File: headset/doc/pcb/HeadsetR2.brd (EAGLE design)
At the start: 85 x 56 mm, 54 parts, among them U1 STM32F405RGT6, U2 MAX17043, U3 MCP73831, U4 MIC5216, U5 MIC5216, U6 MIC5219 3.3V, U7 XBEE, U8 STEVAL-MKI108V2, Y1 8MHz

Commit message: Update headset schematic revision 2 (again), almost ready for route
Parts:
- moved R5 8.91 mm to (81.3, 41.3), turned to 0 degrees
- moved C16 5.99 mm to (75.6, 41.3), turned to 180 degrees
- moved U2 5.68 mm to (72.4, 44.5)
- moved JP3 5.68 mm to (17.8, 43.2), turned to 270 degrees
- moved D1 5.24 mm to (77.5, 44.5), turned to 180 degrees
- moved U3 5.08 mm to (81.9, 45.7)
- moved C21 4.02 mm to (40.6, 52.1)
- moved R6 3.81 mm to (77.5, 47.6), turned to 0 degrees
- moved U5 3.59 mm to (47.6, 50.2), turned to 180 degrees
- moved R1 2.84 mm to (48.3, 40.6), turned to 270 degrees
- moved JP1 2.54 mm to (78.7, 30.5)
- moved C22 2.54 mm to (40.6, 47.0)
- moved C17 2.29 mm to (71.8, 47.6), flipped to the top, turned to 0 degrees
- moved R4 1.27 mm to (71.1, 31.8)
- moved R3 1.27 mm to (71.1, 29.2)
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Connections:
- net !CS!: now also U1.50; no longer U1.33
- net MISO: now also U1.52; no longer U1.35
- net MOSI: now also U1.53; no longer U1.36
- net SCK: now also U1.51; no longer U1.34
- net X_RX: now also U1.16; no longer U1.42
- net X_TX: now also U1.17; no longer U1.43

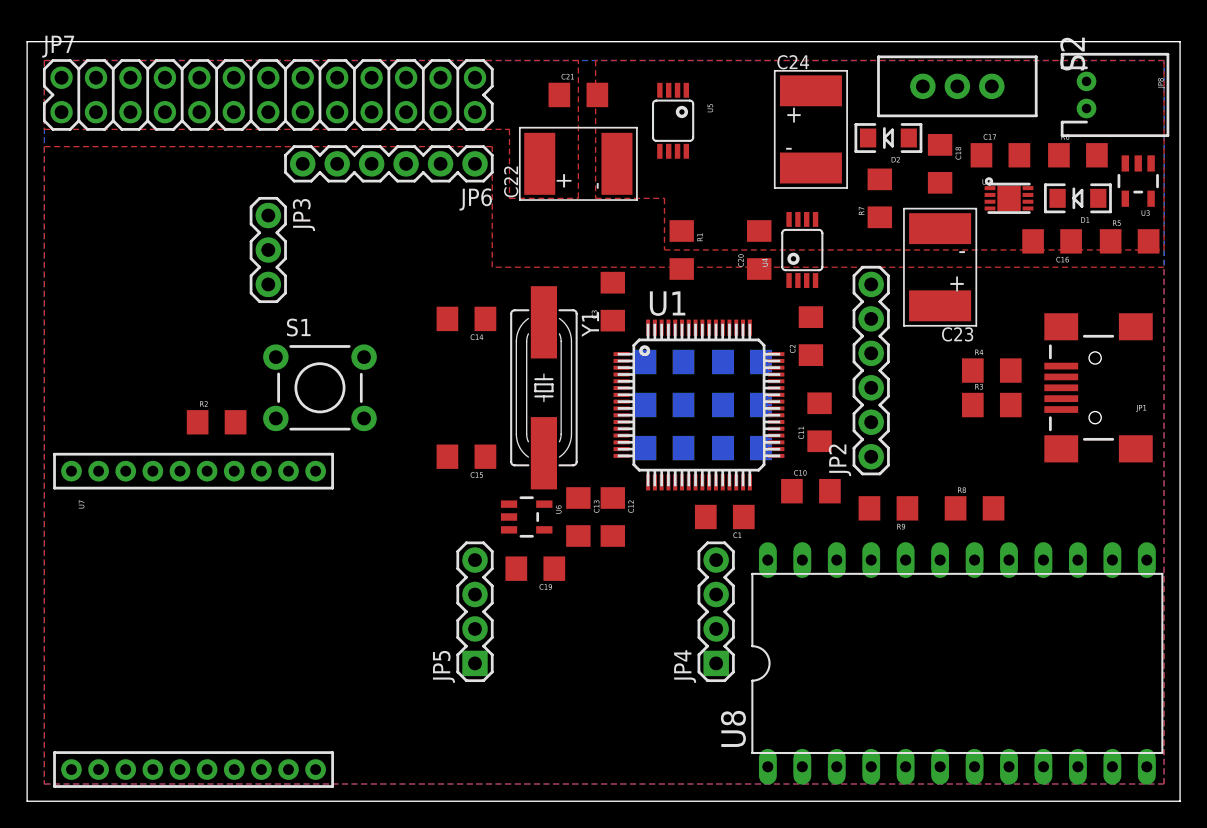
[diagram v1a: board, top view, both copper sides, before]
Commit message: Update schematic revision 2 to fix the issues described in lab notebook
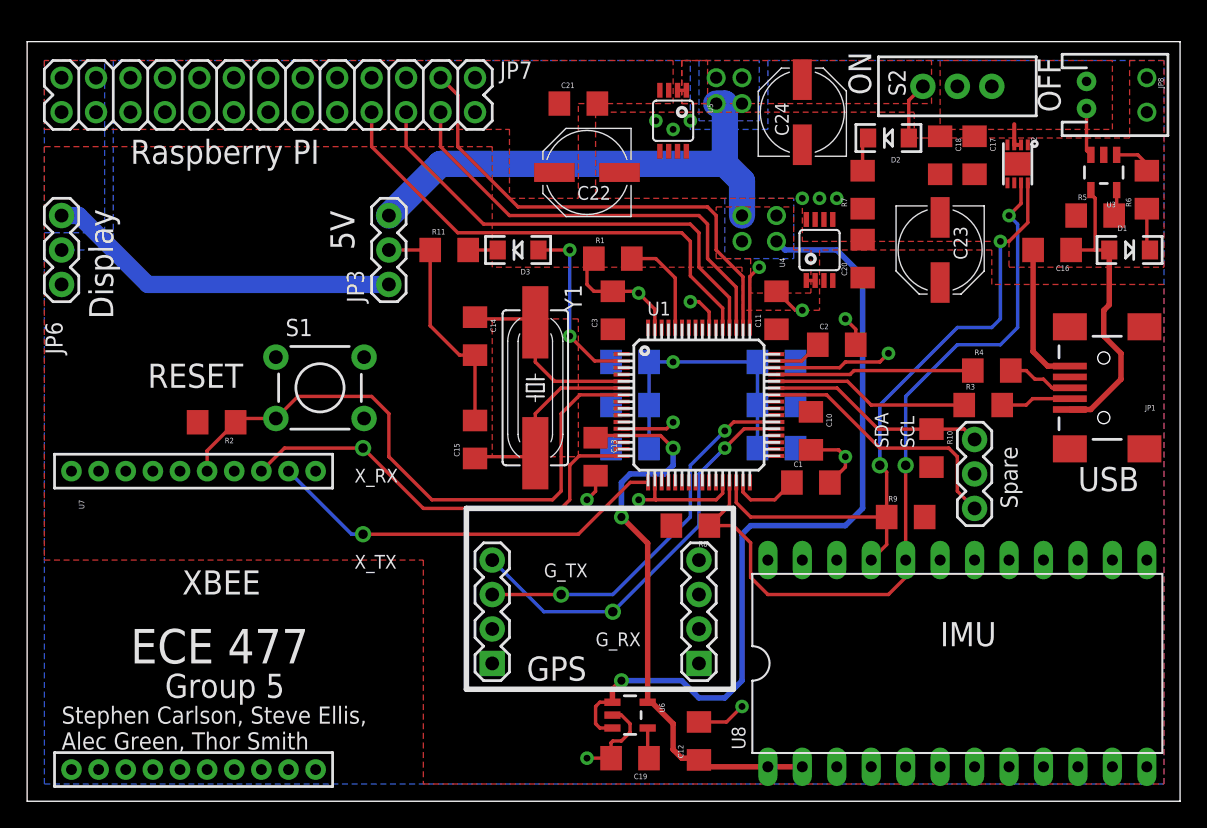
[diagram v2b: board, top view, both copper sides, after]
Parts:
- added D3: LED, SparkFun-LED:LED-1206
- added R10: 10K, ECE477:1206
- added R11: 470, ECE477:1206
- C22, C23, C24: device ECE477:VISHAY_D -> SparkFun-Passives:PANASONIC_D
- JP2: value SWD -> SPARE; device SparkFun-Connectors:1X06 -> SparkFun-Connectors:1X03
- JP6: device SparkFun-Connectors:1X06 -> SparkFun-Connectors:1X03
- moved JP6 31.8 mm to (2.54, 38.1), turned to 90 degrees
- moved R8 21.0 mm to (48.9, 20.3), turned to 180 degrees
- moved C12 17.7 mm to (49.5, 4.45), turned to 90 degrees
- moved JP4 16.5 mm to (34.3, 10.2)
- moved JP5 16.5 mm to (49.5, 10.2)
- moved U6 16.5 mm to (44.5, 6.35)
- moved C19 15.6 mm to (44.5, 3.17)
- moved JP3 10.2 mm to (26.7, 38.1), turned to 90 degrees
- moved C11 8.84 mm to (55.2, 36.2)
- moved JP2 8.52 mm to (69.8, 21.6)
- moved C20 7.65 mm to (61.6, 40.0)
- moved C1 6.84 mm to (57.8, 23.5), turned to 0 degrees
- moved R6 5.68 mm to (82.5, 45.1), turned to 90 degrees
- moved D1 5.39 mm to (81.3, 40.6), turned to 0 degrees
- moved R1 5.12 mm to (43.2, 40.0), turned to 0 degrees
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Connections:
- removed net AGND: C19.2, U1.12, U6.2, U8.13
- new net LED: D3.A, U1.2
- new net LED_LED: D3.C, R11.2
- new net S_RX: JP2.3, R10.1, U1.43
- new net S_TX: JP2.1, U1.42
- net !CS!: no longer JP6.2
- net !RST!: no longer JP2.5
- net 5V: now also JP6.3; no longer JP6.6
- net GND: now also C19.2, JP2.2, R11.1, U1.12, U1.28, U6.2, U8.13; no longer JP2.3
- net MISO: no longer JP6.3
- net MOSI: no longer JP6.4
- net SCK: no longer JP6.5
- net SWCLK: no longer JP2.2
- net SWDIO: no longer JP2.4
- net SWO: no longer JP2.6
- net V_MCU: now also R10.2, U1.57; no longer JP2.1
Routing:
- net V_IN: track 0.00 -> 102.1 mm, vias 0 -> 9
- net GND: track 0.00 -> 72.5 mm, vias 0 -> 17
- net SCL: track 0.00 -> 57.4 mm, vias 0 -> 2
- net SDA: track 0.00 -> 47.9 mm, vias 0 -> 2
- net !RST!: track 0.00 -> 45.3 mm
- net V_ADC: track 0.00 -> 43.3 mm, vias 0 -> 2
- net MOSI: track 0.00 -> 36.3 mm
- net !CS!: track 0.00 -> 35.9 mm
- net MISO: track 0.00 -> 34.7 mm
- net SCK: track 0.00 -> 33.1 mm
- net X_RX: track 0.00 -> 32.2 mm, vias 0 -> 1
- net G_RX: track 0.00 -> 30.3 mm, vias 0 -> 2
- net X_TX: track 0.00 -> 30.0 mm, vias 0 -> 1
- net G_TX: track 0.00 -> 28.4 mm, vias 0 -> 2
- net 5V: track 0.00 -> 26.2 mm
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- added copper zone on layer 16, net 5V
- added copper zone on layer 1, net V_BAT
- added copper zone on layer 1, net V_IN
- added copper zone on layer 16, net V_IN
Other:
- board text added: "5V"
- board text added: "Display"
- board text added: "ECE 477"
- board text added: "GPS"
- board text added: "G_RX"
- board text added: "G_TX"
- board text added: "Group 5"
- board text added: "IMU"
- board text added: "OFF"
- board text added: "ON"
- board text added: "RESET"
- board text added: "Raspberry PI"
- board text added: "SCL"
- board text added: "SDA"
- board text added: "Spare"
- board text added: "Stephen Carlson, Steve Ellis, Alec Green, Thor Smith"
- board text added: "USB"
- board text added: "XBEE"
- board text added: "X_RX"
- board text added: "X_TX"
